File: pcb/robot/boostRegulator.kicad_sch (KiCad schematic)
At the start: 23 parts, among them U5 LSF0102DCTR, U6 MAX77857BEWB+

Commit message: Re-unify USB-PD module into main board (single-PCB architecture) (#17)
Merges the USB-PD module circuitry back into the main robot board as
a single PCB, reversing the earlier main-board/USB-PD-daughter-board
split. Full re-route and re-placement of the combined design:

- Consolidated low-profile parts toward the board center, using the
  space freed up by relocated capacitors, for better overall use of
  the available area.
- Kept all 0-ohm test/isolation jumpers in accessible locations for
  bench testing.
- Added/corrected footprints for several parts that had broken or
  incorrect footprints (DDC6_TEX variants, SOT-23-6, SOT-23-3,
  R0402).

Carries forward every closed correction issue and update made since
the original split: #3 (CC jumpers), #6 (IC1.ON pull-down), #14/#15
(ADC divider, motor connector pinout), #16, #18 (I2C isolation
jumpers), #19 (charger-sense GPIO interrupt), plus the BOM/pricing
updates, LED changes, and MAX77642 replacement.

Verified via kicad-cli ERC/DRC + netlist diff against the pre-merge
board: 0 unconnected items (unchanged), no new DRC error-level
violations besides one pre-existing excluded item, and the #6
(IC1.ON pull-down) and #19 (charger-sense GPIO interrupt) circuits
confirmed intact at the net-topology level despite the full-board
re-annotation changing most reference designators. Most of the raw
diff size is a KiCad 9 footprint-format upgrade (pre-2023 format
rewritten to current) rather than design changes - spot-checked
against unrelated footprints (e.g. mounting holes), which show
identical geometry under the new syntax.
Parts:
- NT14: renamed from NT15; symbol Device:NetTie_2 -> robot:NetTie_2
- R69: renamed from R53; symbol Device:R -> robot:R
- R70: renamed from R40; symbol Device:R -> robot:R
- renumbered C24 to C33, C25 to C38, C27 to C39, C26 to C40, C29 to C41, C28 to C43, C30 to C46, C31 to C48, C32 to C51, C33 to C52, C34 to C55, C91 to C57, L1 to L3, R19 to R66, R20 to R71, R21 to R72, TP18 to TP27, TP19 to TP28, U5 to U21, U6 to U23
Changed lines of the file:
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@@
 		(on_board yes)
 		(dnp no)
-		(property "Reference" "U6"
+		(property "Reference" "U23"
 			(at 194.31 104.14 0)
 			(effects
@@
 			(project "robot"
 				(path "/0c7b298e-2d07-4b1f-b033-e95f02d45089/427922e5-a943-4728-8788-709c0c3b2395"
-					(reference "U6")
+					(reference "U23")
 					(unit 1)
 				)
@@
 		(on_board yes)
 		(dnp no)
-		(property "Reference" "C28"
+		(property "Reference" "C43"
 			(at 160.02 113.0299 0)
 			(effects
@@
 			(project "robot"
 				(path "/0c7b298e-2d07-4b1f-b033-e95f02d45089/427922e5-a943-4728-8788-709c0c3b2395"
-					(reference "C28")
+					(reference "C43")
 					(unit 1)
 				)
@@
 		(dnp no)
 		(fields_autoplaced yes)
-		(property "Reference" "U5"
+		(property "Reference" "U21"
 			(at 78.74 109.22 0)
 			(effects
@@
 			(project "robot"
 				(path "/0c7b298e-2d07-4b1f-b033-e95f02d45089/427922e5-a943-4728-8788-709c0c3b2395"
-					(reference "U5")
+					(reference "U21")
 					(unit 1)
 				)
@@
 	)
 	(symbol
-		(lib_id "Device:NetTie_2")
+		(lib_id "robot:NetTie_2")
 		(at 218.44 104.775 270)
 		(unit 1)
@@
 		(on_board yes)
 		(dnp no)
-		(property "Reference" "NT15"
+		(property "Reference" "NT14"
 			(at 220.345 103.505 90)
 			(effects
@@
 			(project "robot"
 				(path "/0c7b298e-2d07-4b1f-b033-e95f02d45089/427922e5-a943-4728-8788-709c0c3b2395"
-					(reference "NT15")
+					(reference "NT14")
 					(unit 1)
 				)
@@
 		(on_board yes)
 		(dnp no)
-		(property "Reference" "C32"
+		(property "Reference" "C51"
 			(at 223.52 95.25 0)
 			(effects
@@
 			(project "robot"
 				(path "/0c7b298e-2d07-4b1f-b033-e95f02d45089/427922e5-a943-4728-8788-709c0c3b2395"
-					(reference "C32")
+					(reference "C51")
 					(unit 1)
 				)
@@
 		(on_board yes)
 		(dnp no)
-		(property "Reference" "C27"
+		(property "Reference" "C39"
 			(at 141.605 91.4399 0)
 			(effects
@@
 			(project "robot"
 				(path "/0c7b298e-2d07-4b1f-b033-e95f02d45089/427922e5-a943-4728-8788-709c0c3b2395"
-					(reference "C27")
+					(reference "C39")
 					(unit 1)
 				)
@@
 	)
 	(symbol
-		(lib_id "Device:R")
+		(lib_id "robot:R")
 		(at 105.41 129.54 90)
 		(unit 1)
@@
 		(on_board yes)
 		(dnp no)
-		(property "Reference" "R40"
+		(property "Reference" "R70"
 			(at 105.664 131.826 90)
 			(effects
@@
 			(project "robot"
 				(path "/0c7b298e-2d07-4b1f-b033-e95f02d45089/427922e5-a943-4728-8788-709c0c3b2395"
-					(reference "R40")
+					(reference "R70")
 					(unit 1)
 				)
@@
 		(on_board yes)
 		(dnp no)
-		(property "Reference" "R20"
+		(property "Reference" "R71"
 			(at 114.935 114.2999 0)
 			(effects
@@
 			(project "robot"
 				(path "/0c7b298e-2d07-4b1f-b033-e95f02d45089/427922e5-a943-4728-8788-709c0c3b2395"
-					(reference "R20")
+					(reference "R71")
 					(unit 1)
 				)
@@
 		(dnp no)
 		(fields_autoplaced yes)
-		(property "Reference" "C25"
+		(property "Reference" "C38"
 			(at 128.905 91.4399 0)
 			(effects
@@
 			(project "robot"
 				(path "/0c7b298e-2d07-4b1f-b033-e95f02d45089/427922e5-a943-4728-8788-709c0c3b2395"
-					(reference "C25")
+					(reference "C38")
 					(unit 1)
 				)
@@
 		(on_board yes)
 		(dnp no)
-		(property "Reference" "C24"
+		(property "Reference" "C33"
 			(at 48.26 119.3799 0)
 			(effects
@@
 			(project "robot"
 				(path "/0c7b298e-2d07-4b1f-b033-e95f02d45089/427922e5-a943-4728-8788-709c0c3b2395"
-					(reference "C24")
+					(reference "C33")
 					(unit 1)
 				)
@@
 		(on_board yes)
 		(dnp no)
-		(property "Reference" "C29"
+		(property "Reference" "C41"
 			(at 158.115 91.44 0)
 			(effects
@@
 			(project "robot"
 				(path "/0c7b298e-2d07-4b1f-b033-e95f02d45089/427922e5-a943-4728-8788-709c0c3b2395"
-					(reference "C29")
+					(reference "C41")
 					(unit 1)
 				)
@@
 		(on_board yes)
 		(dnp no)
-		(property "Reference" "TP19"
+		(property "Reference" "TP28"
 			(at 98.552 134.112 0)
 			(effects
@@
 			(project "robot"
 				(path "/0c7b298e-2d07-4b1f-b033-e95f02d45089/427922e5-a943-4728-8788-709c0c3b2395"
-					(reference "TP19")
+					(reference "TP28")
 					(unit 1)
 				)
@@
 		(on_board yes)
 		(dnp no)
-		(property "Reference" "C34"
+		(property "Reference" "C55"
 			(at 248.92 95.25 0)
 			(effects
@@
 			(project "robot"
 				(path "/0c7b298e-2d07-4b1f-b033-e95f02d45089/427922e5-a943-4728-8788-709c0c3b2395"
-					(reference "C34")
+					(reference "C55")
 					(unit 1)
 				)
@@
 		(dnp no)
 		(fields_autoplaced yes)
-		(property "Reference" "L1"
+		(property "Reference" "L3"
 			(at 195.58 67.31 90)
 			(effects
@@
 			(project "robot"
 				(path "/0c7b298e-2d07-4b1f-b033-e95f02d45089/427922e5-a943-4728-8788-709c0c3b2395"
-					(reference "L1")
+					(reference "L3")
 					(unit 1)
 				)
@@
 		(on_board yes)
 		(dnp no)
-		(property "Reference" "C33"
+		(property "Reference" "C52"
 			(at 236.22 95.25 0)
 			(effects
@@
 			(project "robot"
 				(path "/0c7b298e-2d07-4b1f-b033-e95f02d45089/427922e5-a943-4728-8788-709c0c3b2395"
-					(reference "C33")
+					(reference "C52")
 					(unit 1)
 				)
@@
 		(on_board yes)
 		(dnp no)
-		(property "Reference" "C30"
+		(property "Reference" "C46"
 			(at 184.15 66.04 90)
 			(effects
@@
 			(project "robot"
 				(path "/0c7b298e-2d07-4b1f-b033-e95f02d45089/427922e5-a943-4728-8788-709c0c3b2395"
-					(reference "C30")
+					(reference "C46")
 					(unit 1)
 				)
@@
 		(on_board yes)
 		(dnp no)
-		(property "Reference" "TP18"
+		(property "Reference" "TP27"
 			(at 100.33 122.428 0)
 			(effects
@@
 			(project "robot"
 				(path "/0c7b298e-2d07-4b1f-b033-e95f02d45089/427922e5-a943-4728-8788-709c0c3b2395"
-					(reference "TP18")
+					(reference "TP27")
 					(unit 1)
 				)
@@
 		(dnp no)
 		(fields_autoplaced yes)
-		(property "Reference" "R19"
+		(property "Reference" "R66"
 			(at 59.69 119.3799 0)
 			(effects
@@
 			(project "robot"
 				(path "/0c7b298e-2d07-4b1f-b033-e95f02d45089/427922e5-a943-4728-8788-709c0c3b2395"
-					(reference "R19")
+					(reference "R66")
 					(unit 1)
 				)
@@
 		(on_board yes)
 		(dnp no)
-		(property "Reference" "C26"
+		(property "Reference" "C40"
 			(at 148.59 106.6799 0)
 			(effects
@@
 			(project "robot"
 				(path "/0c7b298e-2d07-4b1f-b033-e95f02d45089/427922e5-a943-4728-8788-709c0c3b2395"
-					(reference "C26")
+					(reference "C40")
 					(unit 1)
 				)
@@
 	)
 	(symbol
-		(lib_id "Device:R")
+		(lib_id "robot:R")
 		(at 105.41 127 90)
 		(unit 1)
@@
 		(on_board yes)
 		(dnp no)
-		(property "Reference" "R53"
+		(property "Reference" "R69"
 			(at 105.41 124.46 90)
 			(effects
@@
 			(project "robot"
 				(path "/0c7b298e-2d07-4b1f-b033-e95f02d45089/427922e5-a943-4728-8788-709c0c3b2395"
-					(reference "R53")
+					(reference "R69")
 					(unit 1)
 				)
@@
 		(on_board yes)
 		(dnp no)
-		(property "Reference" "C31"
+		(property "Reference" "C48"
 			(at 205.74 66.04 90)
 			(effects
@@
 			(project "robot"
 				(path "/0c7b298e-2d07-4b1f-b033-e95f02d45089/427922e5-a943-4728-8788-709c0c3b2395"
-					(reference "C31")
+					(reference "C48")
 					(unit 1)
 				)
@@
 		(dnp no)
 		(fields_autoplaced yes)
-		(property "Reference" "R21"
+		(property "Reference" "R72"
 			(at 123.825 114.2999 0)
 			(effects
@@
 			(project "robot"
 				(path "/0c7b298e-2d07-4b1f-b033-e95f02d45089/427922e5-a943-4728-8788-709c0c3b2395"
-					(reference "R21")
+					(reference "R72")
 					(unit 1)
 				)
@@
 		(on_board yes)
 		(dnp yes)
-		(property "Reference" "C91"
+		(property "Reference" "C57"
 			(at 262.89 91.4399 0)
 			(effects
@@
 			(project "robot"
 				(path "/0c7b298e-2d07-4b1f-b033-e95f02d45089/427922e5-a943-4728-8788-709c0c3b2395"
-					(reference "C91")
+					(reference "C57")
 					(unit 1)
 				)

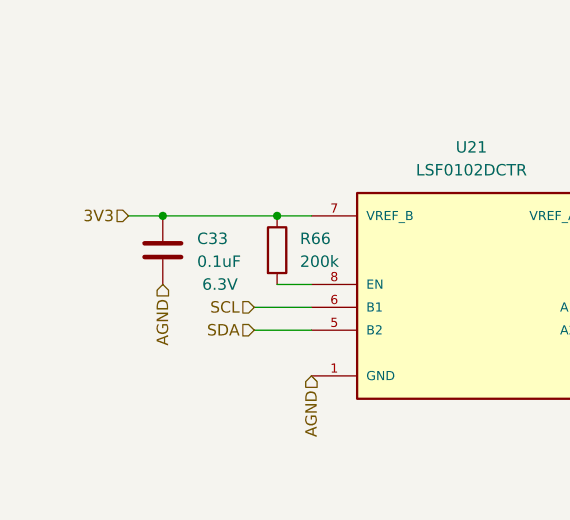
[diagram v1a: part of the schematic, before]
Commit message: Add isolation jumper for U21 (fixes #18)
Added R122/R123, same 0-ohm/0603 pattern as the other 10 jumpers - one on I2C0_SCL, one on I2C0_SDA, right at U21's pins, so it can be pulled off the bus during debugging like the rest of the slaves. ERC/DRC clean.
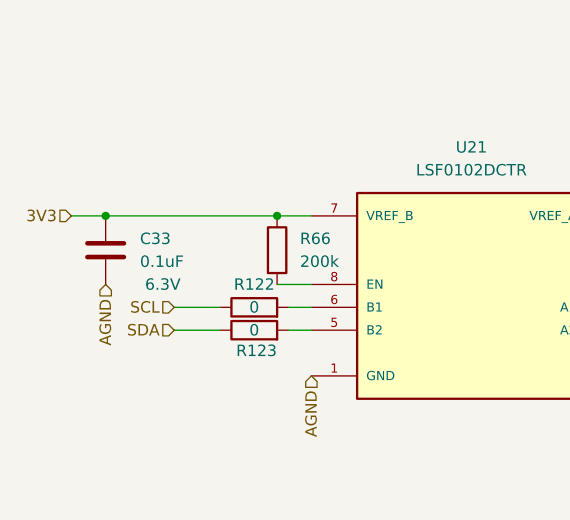
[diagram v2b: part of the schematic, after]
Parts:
- added R122, R123: 0, robot:R_0603_1608Metric, symbol robot:R
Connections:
- net SCL: now also R122.1; no longer U21.6 (B1)
- net SDA: now also R123.1; no longer U21.5 (B2)
- new net: R123.2, U21.5 (B2)
- new net: R122.2, U21.6 (B1)
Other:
- moved on the sheet: C33

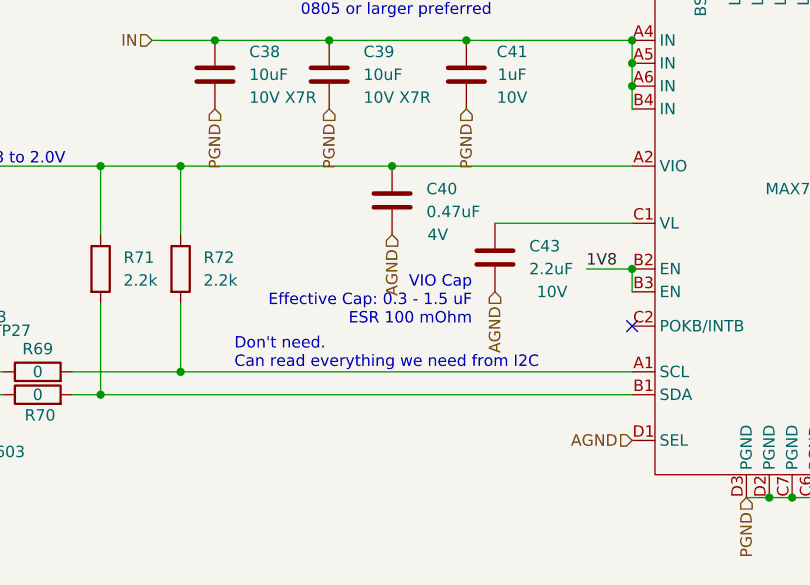
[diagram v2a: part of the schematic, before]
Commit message: Gate MAX77857 EN via GPIO22 divider, bump C136 to 100nF (#24)
R135/R136 (10k/10k) now gate U23.EN from GPIO22 instead of tying it
straight to 1.8V. GPIO22 low or floating (RP2040 reset/boot default)
holds EN at 0V, no firmware dependency for the off-state. VIO stays
on 1.8V, untouched. C136 220pF -> 100nF (CL05A104KA5NNNC) to meet
the MAX6006's real >=10nF minimum.

Verified against baseline: ERC 337/337 (no new violations), DRC 0
unconnected items, no violations tied to the new parts.
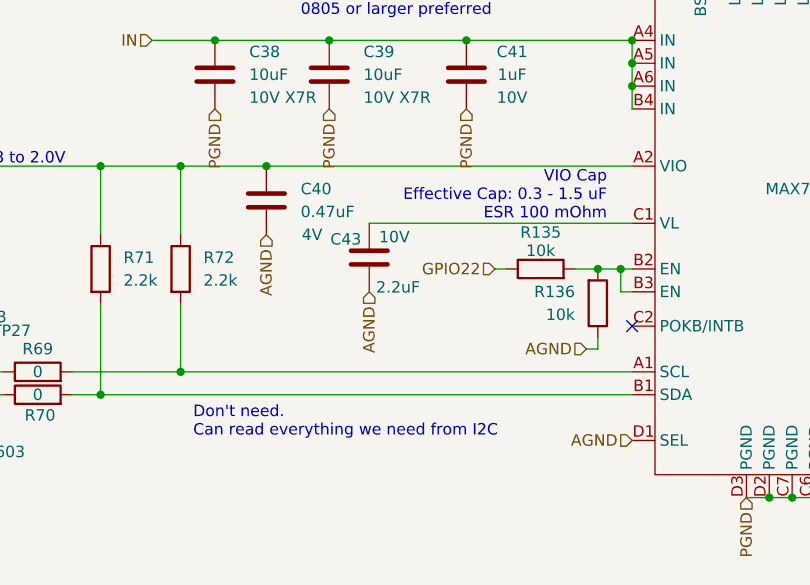
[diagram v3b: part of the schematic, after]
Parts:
- added R135, R136: 10k, robot:R_0603_1608Metric, symbol robot:R
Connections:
- net 1V8: no longer U23.B2 (EN), U23.B3 (EN)
- net AGND: now also R136.1
- new net: R135.2, R136.2, U23.B2 (EN), U23.B3 (EN)
- new net GPIO22: R135.1
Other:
- moved on the sheet: C40, C43
